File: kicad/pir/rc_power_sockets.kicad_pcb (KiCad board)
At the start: 2 copper layers, 50 x 50 mm, 32 parts, among them IC1 ATTINY85, J1 PIR, J2 433MHZ, J3 433MHZ, P1 ICSP, P2 ALT_PWR, Q1 NMOS, Q2 PMOS, SW1 SWITCH_INV, U1 MCP1755ST-3302E/DB

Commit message: Corrected the PMOS
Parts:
- R2: value 10K -> 100K
- moved Q2 6.33 mm to (130.4, 93.5), turned to 0 degrees
- moved R2 2.94 mm to (130.0, 98.1), turned to 180 degrees
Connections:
- Q2 pad 2: /SWITCH_POWER -> /POWER
- Q2 pad 3: /POWER -> /SWITCH_POWER
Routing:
- net /PBASE: track 30.3 -> 26.5 mm, vias 2 -> 0
- net /POWER: track 28.7 -> 25.2 mm
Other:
- board text added: "RC Power Sockets v1.1 - Sept 2016"
- board text removed: "RC Power Sockets v1.0 - March 2016"
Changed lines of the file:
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@@
     (links 58)
     (no_connects 0)
-    (area 116.525 58.475 171.308334 111.375)
+    (area 119.924999 59.924999 170.075001 110.075001)
     (thickness 1.6)
     (drawings 47)
-    (tracks 281)
+    (tracks 277)
     (zones 0)
     (modules 32)
@@
   )
   (module TO_SOT_Packages_SMD:SOT-23_Handsoldering (layer F.Cu)
-    (at 124.5 95.9 180)
+    (at 130.355 93.503)
     (descr "SOT-23, Handsoldering")
     (tags SOT-23)
     (attr smd)
-    (fp_text reference Q2 (at 0 4 180) (layer F.SilkS) hide
-      (effects (font (size 1 1) (thickness 0.15)))
-    )
-    (fp_text value PMOS (at 0.1 -3.6 180) (layer F.SilkS)
+    (fp_text reference Q2 (at 0 4) (layer F.SilkS) hide
+      (effects (font (size 1 1) (thickness 0.15)))
+    )
+    (fp_text value PMOS (at 0.1 -3.6) (layer F.SilkS)
       (effects (font (size 1 1) (thickness 0.15)))
     )
@@
     (fp_line (start 1.29916 -0.65024) (end 1.49982 -0.65024) (layer F.SilkS) (width 0.15))
     (fp_line (start 1.49982 -0.65024) (end 1.49982 0.0508) (layer F.SilkS) (width 0.15))
-    (pad 1 smd rect (at -0.95 1.50114 180) (size 0.8001 1.80086) (layers F.Cu F.Paste F.Mask)
+    (pad 1 smd rect (at -0.95 1.50114) (size 0.8001 1.80086) (layers F.Cu F.Paste F.Mask)
       (net 11 /PBASE))
-    (pad 2 smd rect (at 0.95 1.50114 180) (size 0.8001 1.80086) (layers F.Cu F.Paste F.Mask)
+    (pad 2 smd rect (at 0.95 1.50114) (size 0.8001 1.80086) (layers F.Cu F.Paste F.Mask)
+      (net 13 /POWER))
+    (pad 3 smd rect (at 0 -1.50114) (size 0.8001 1.80086) (layers F.Cu F.Paste F.Mask)
       (net 8 /SWITCH_POWER))
-    (pad 3 smd rect (at 0 -1.50114 180) (size 0.8001 1.80086) (layers F.Cu F.Paste F.Mask)
-      (net 13 /POWER))
     (model TO_SOT_Packages_SMD.3dshapes/SOT-23_Handsoldering.wrl
       (at (xyz 0 0 0))
@@
   )
   (module Resistors_SMD:R_0805_HandSoldering (layer F.Cu)
-    (at 128 95.9 90)
+    (at 129.974 98.075 180)
     (descr "Resistor SMD 0805, hand soldering")
     (tags "resistor 0805")
     (attr smd)
-    (fp_text reference R2 (at 0 2.2 180) (layer F.SilkS)
-      (effects (font (size 1 1) (thickness 0.15)))
-    )
-    (fp_text value 10K (at 3.4 0 180) (layer F.SilkS)
+    (fp_text reference R2 (at 3.556 0 360) (layer F.SilkS)
+      (effects (font (size 1 1) (thickness 0.15)))
+    )
+    (fp_text value 100K (at 0 -2.032 360) (layer F.SilkS)
       (effects (font (size 1 1) (thickness 0.15)))
     )
@@
     (fp_line (start 0.6 0.875) (end -0.6 0.875) (layer F.SilkS) (width 0.15))
     (fp_line (start -0.6 -0.875) (end 0.6 -0.875) (layer F.SilkS) (width 0.15))
-    (pad 1 smd rect (at -1.35 0 90) (size 1.5 1.3) (layers F.Cu F.Paste F.Mask)
+    (pad 1 smd rect (at -1.35 0 180) (size 1.5 1.3) (layers F.Cu F.Paste F.Mask)
       (net 13 /POWER))
-    (pad 2 smd rect (at 1.35 0 90) (size 1.5 1.3) (layers F.Cu F.Paste F.Mask)
+    (pad 2 smd rect (at 1.35 0 180) (size 1.5 1.3) (layers F.Cu F.Paste F.Mask)
       (net 11 /PBASE))
     (model Resistors_SMD.3dshapes/R_0805_HandSoldering.wrl
@@
     (effects (font (size 1 1) (thickness 0.15)) (justify mirror))
   )
-  (gr_text "RC Power Sockets v1.0  - March 2016" (at 144.6 61.3) (layer B.SilkS)
+  (gr_text "RC Power Sockets v1.1  - Sept 2016" (at 144.6 61.3) (layer B.SilkS)
     (effects (font (size 1 1) (thickness 0.15) italic) (justify mirror))
   )
@@
   (segment (start 165.28 97.44) (end 167.82 97.44) (width 0.406) (layer F.Cu) (net 7))
   (segment (start 162.4 94.56) (end 165.28 97.44) (width 0.406) (layer F.Cu) (net 7))
+  (segment (start 126 89.9) (end 128.10186 92.00186) (width 0.813) (layer F.Cu) (net 8))
+  (segment (start 128.10186 92.00186) (end 130.355 92.00186) (width 0.813) (layer F.Cu) (net 8))
   (segment (start 152.45 71.5) (end 152.45 73.44) (width 0.813) (layer F.Cu) (net 8))
   (segment (start 140.896 64.42) (end 137.34 64.42) (width 0.813) (layer F.Cu) (net 8))
@@
   (segment (start 155.5 70.588) (end 155.464 70.552) (width 0.813) (layer F.Cu) (net 8))
   (segment (start 126 84.698) (end 126 89.9) (width 0.813) (layer F.Cu) (net 8))
-  (segment (start 123.55 92.35) (end 123.55 94.39886) (width 0.813) (layer F.Cu) (net 8))
-  (segment (start 126 89.9) (end 123.55 92.35) (width 0.813) (layer F.Cu) (net 8))
   (segment (start 126 84.698) (end 126 84.838) (width 0.813) (layer F.Cu) (net 8))
   (segment (start 126 84.838) (end 126 81.4) (width 0.813) (layer F.Cu) (net 8))
@@
   (segment (start 144.44886 101.9) (end 144.15 102.19886) (width 0.406) (layer F.Cu) (net 10))
   (segment (start 147.05 105.1) (end 147.05 101.9) (width 0.406) (layer F.Cu) (net 10))
-  (segment (start 128 94.55) (end 130.55 94.55) (width 0.406) (layer F.Cu) (net 11))
-  (segment (start 143.2 106.9) (end 143.2 105.20114) (width 0.406) (layer F.Cu) (net 11))
-  (segment (start 142.4 107.7) (end 143.2 106.9) (width 0.406) (layer F.Cu) (net 11))
-  (segment (start 135.4 107.7) (end 142.4 107.7) (width 0.406) (layer F.Cu) (net 11))
-  (segment (start 133.4 105.7) (end 135.4 107.7) (width 0.406) (layer F.Cu) (net 11))
-  (via (at 133.4 105.7) (size 0.75) (drill 0.4) (layers F.Cu B.Cu) (net 11))
-  (segment (start 130.6 102.9) (end 133.4 105.7) (width 0.406) (layer B.Cu) (net 11))
-  (segment (start 130.6 101.3) (end 130.6 102.9) (width 0.406) (layer B.Cu) (net 11))
-  (segment (start 130.6 94.5) (end 130.6 101.3) (width 0.406) (layer B.Cu) (net 11))
-  (via (at 130.6 94.5) (size 0.75) (drill 0.4) (layers F.Cu B.Cu) (net 11))
-  (segment (start 130.55 94.55) (end 130.6 94.5) (width 0.406) (layer F.Cu) (net 11))
-  (segment (start 125.45 94.39886) (end 127.84886 94.39886) (width 0.406) (layer F.Cu) (net 11))
-  (segment (start 127.84886 94.39886) (end 128 94.55) (width 0.406) (layer F.Cu) (net 11))
+  (segment (start 143.2 105.20114) (end 143.2 106.9) (width 0.406) (layer F.Cu) (net 11))
+  (segment (start 143.2 106.9) (end 142.4 107.7) (width 0.406) (layer F.Cu) (net 11))
+  (segment (start 142.4 107.7) (end 134.031 107.7) (width 0.406) (layer F.Cu) (net 11))
+  (segment (start 134.031 107.7) (end 128.624 102.293) (width 0.406) (layer F.Cu) (net 11))
+  (segment (start 128.624 102.293) (end 128.624 98.075) (width 0.406) (layer F.Cu) (net 11))
+  (segment (start 129.413 96.23) (end 129.413 95.01214) (width 0.406) (layer F.Cu) (net 11))
+  (segment (start 129.413 95.01214) (end 129.405 95.00414) (width 0.406) (layer F.Cu) (net 11))
+  (segment (start 128.624 98.075) (end 128.624 97.019) (width 0.406) (layer F.Cu) (net 11))
+  (segment (start 128.624 97.019) (end 129.413 96.23) (width 0.406) (layer F.Cu) (net 11))
   (segment (start 157 105.4336) (end 158.016 105.4336) (width 0.406) (layer F.Cu) (net 12))
   (segment (start 158.016 105.4336) (end 161.724 101.7256) (width 0.406) (layer F.Cu) (net 12))
@@
   (segment (start 155.141 105.441) (end 151.6 101.9) (width 0.406) (layer F.Cu) (net 12))
   (segment (start 151.6 101.9) (end 149.75 101.9) (width 0.406) (layer F.Cu) (net 12))
+  (segment (start 131.324 98.075) (end 131.324 95.02314) (width 0.813) (layer F.Cu) (net 13))
+  (segment (start 131.324 95.02314) (end 131.305 95.00414) (width 0.813) (layer F.Cu) (net 13))
+  (segment (start 136.959 95.027) (end 133.911 98.075) (width 0.813) (layer F.Cu) (net 13))
+  (segment (start 133.911 98.075) (end 131.324 98.075) (width 0.813) (layer F.Cu) (net 13))
+  (segment (start 136.959 92.36) (end 136.959 95.027) (width 0.813) (layer F.Cu) (net 13))
   (segment (start 147.5 94.9) (end 147.5 93.249) (width 0.813) (layer F.Cu) (net 13))
   (segment (start 147.5 93.249) (end 146.611 92.36) (width 0.813) (layer F.Cu) (net 13))
   (segment (start 146.611 92.36) (end 136.959 92.36) (width 0.813) (layer F.Cu) (net 13))
-  (segment (start 136.959 92.36) (end 136.959 95.027) (width 0.813) (layer F.Cu) (net 13))
-  (segment (start 136.959 95.027) (end 134.736 97.25) (width 0.813) (layer F.Cu) (net 13))
-  (segment (start 134.736 97.25) (end 128 97.25) (width 0.813) (layer F.Cu) (net 13))
-  (segment (start 124.5 97.40114) (end 127.84886 97.40114) (width 0.813) (layer F.Cu) (net 13))
-  (segment (start 127.84886 97.40114) (end 128 97.25) (width 0.813) (layer F.Cu) (net 13))
   (segment (start 168 73.94902) (end 165.80098 73.94902) (width 0.406) (layer B.Cu) (net 14))
   (segment (start 165.80098 73.94902) (end 165.5 74.25) (width 0.406) (layer B.Cu) (net 14))

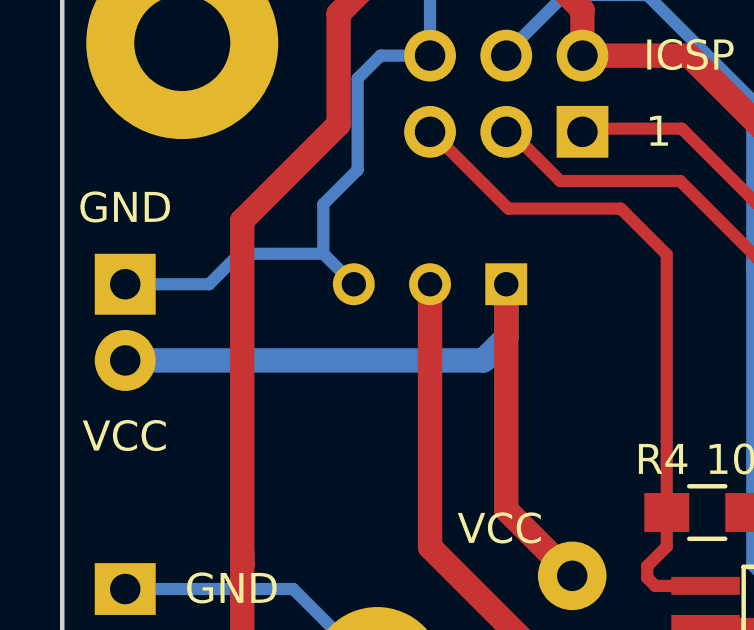
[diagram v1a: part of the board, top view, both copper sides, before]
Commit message: Capacitor on the power input
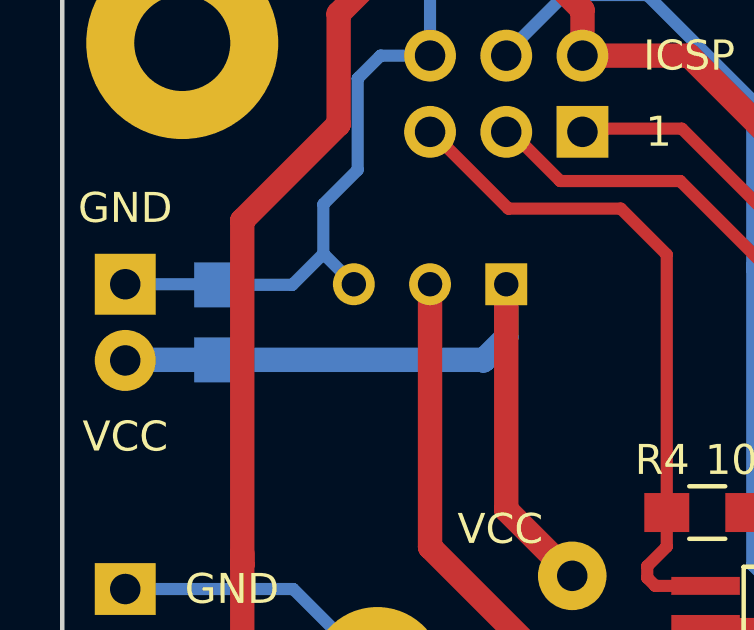
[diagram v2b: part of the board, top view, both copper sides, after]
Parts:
- added C4: 10uF, Capacitors_SMD:C_0805_HandSoldering, B.Cu at (125.0, 73.3)
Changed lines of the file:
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@@
 (kicad_pcb (version 4) (host pcbnew 4.0.1-stable)
   (general
-    (links 58)
+    (links 60)
     (no_connects 0)
     (area 119.924999 59.924999 170.075001 110.075001)
     (thickness 1.6)
     (drawings 47)
-    (tracks 277)
+    (tracks 282)
     (zones 0)
-    (modules 32)
+    (modules 33)
     (nets 18)
   )
@@
       (net 17 /VCC_SWITCHED))
   )
+  (module Capacitors_SMD:C_0805_HandSoldering (layer B.Cu)
+    (at 125.021 73.31 90)
+    (descr "Capacitor SMD 0805, hand soldering")
+    (tags "capacitor 0805")
+    (attr smd)
+    (fp_text reference C4 (at 3.048 0 180) (layer B.SilkS)
+      (effects (font (size 1 1) (thickness 0.15)) (justify mirror))
+    )
+    (fp_text value 10uF (at 0 1.778 90) (layer B.SilkS)
+      (effects (font (size 1 1) (thickness 0.15)) (justify mirror))
+    )
+    (fp_line (start -2.3 1) (end 2.3 1) (layer B.CrtYd) (width 0.05))
+    (fp_line (start -2.3 -1) (end 2.3 -1) (layer B.CrtYd) (width 0.05))
+    (fp_line (start -2.3 1) (end -2.3 -1) (layer B.CrtYd) (width 0.05))
+    (fp_line (start 2.3 1) (end 2.3 -1) (layer B.CrtYd) (width 0.05))
+    (fp_line (start 0.5 0.85) (end -0.5 0.85) (layer B.SilkS) (width 0.15))
+    (fp_line (start -0.5 -0.85) (end 0.5 -0.85) (layer B.SilkS) (width 0.15))
+    (pad 1 smd rect (at -1.25 0 90) (size 1.5 1.25) (layers B.Cu B.Paste B.Mask)
+      (net 16 VCC))
+    (pad 2 smd rect (at 1.25 0 90) (size 1.5 1.25) (layers B.Cu B.Paste B.Mask)
+      (net 1 GND))
+    (model Capacitors_SMD.3dshapes/C_0805_HandSoldering.wrl
+      (at (xyz 0 0 0))
+      (scale (xyz 1 1 1))
+      (rotate (xyz 0 0 0))
+    )
+  )
   (gr_text POT (at 167.693 92.36) (layer F.SilkS)
     (effects (font (size 1 1) (thickness 0.15)))
@@
     (effects (font (size 1 1) (thickness 0.15)) (justify mirror))
   )
-  (gr_text "RC Power Sockets v1.1  - Sept 2016" (at 144.6 61.3) (layer B.SilkS)
+  (gr_text "RC Power Sockets v1.1 - Sept 2016" (at 144.6 61.3) (layer B.SilkS)
     (effects (font (size 1 1) (thickness 0.15) italic) (justify mirror))
   )
@@
   (gr_line (start 170 60) (end 170 110) (angle 90) (layer Edge.Cuts) (width 0.15))
   (gr_line (start 120 60) (end 170 60) (angle 90) (layer Edge.Cuts) (width 0.15))
+  (segment (start 125.021 72.06) (end 127.668 72.06) (width 0.406) (layer B.Cu) (net 1))
+  (segment (start 127.668 72.06) (end 128.704 71.024) (width 0.406) (layer B.Cu) (net 1))
+  (segment (start 122.1 72.04) (end 125.001 72.04) (width 0.406) (layer B.Cu) (net 1))
+  (segment (start 125.001 72.04) (end 125.021 72.06) (width 0.406) (layer B.Cu) (net 1))
+  (segment (start 124.894 72.04) (end 124.914 72.06) (width 0.406) (layer B.Cu) (net 1))
   (segment (start 141.825 85.905) (end 139.477 85.905) (width 0.406) (layer F.Cu) (net 1))
   (segment (start 139.477 85.905) (end 138.991 86.391) (width 0.406) (layer F.Cu) (net 1))
@@
   (segment (start 135.701 90.201) (end 134.177 88.677) (width 0.406) (layer F.Cu) (net 1))
   (segment (start 129.72 72.04) (end 128.704 71.024) (width 0.406) (layer B.Cu) (net 1))
-  (segment (start 128.704 71.024) (end 125.91 71.024) (width 0.406) (layer B.Cu) (net 1))
-  (segment (start 124.894 72.04) (end 122.1 72.04) (width 0.406) (layer B.Cu) (net 1))
-  (segment (start 125.91 71.024) (end 124.894 72.04) (width 0.406) (layer B.Cu) (net 1))
   (segment (start 130.609 64.42) (end 132.26 64.42) (width 0.406) (layer B.Cu) (net 1))
   (segment (start 129.847 65.182) (end 130.609 64.42) (width 0.406) (layer B.Cu) (net 1))
@@
   (segment (start 146.8 102) (end 137 102) (width 0.813) (layer B.Cu) (net 15))
   (segment (start 152 96.8) (end 146.8 102) (width 0.813) (layer B.Cu) (net 15))
+  (segment (start 134.038 74.58) (end 134.018 74.56) (width 0.813) (layer B.Cu) (net 16))
+  (segment (start 134.018 74.56) (end 125.021 74.56) (width 0.813) (layer B.Cu) (net 16))
+  (segment (start 125.021 74.56) (end 122.12 74.56) (width 0.813) (layer B.Cu) (net 16))
+  (segment (start 122.12 74.56) (end 122.1 74.58) (width 0.813) (layer B.Cu) (net 16))
   (segment (start 134.8 72.04) (end 134.8 79.56) (width 0.813) (layer F.Cu) (net 16))
   (segment (start 134.8 79.56) (end 137 81.76) (width 0.813) (layer F.Cu) (net 16))
-  (segment (start 122.1 74.58) (end 134.038 74.58) (width 0.813) (layer B.Cu) (net 16))
   (segment (start 134.8 73.818) (end 134.8 72.04) (width 0.813) (layer B.Cu) (net 16))
   (segment (start 134.038 74.58) (end 134.8 73.818) (width 0.813) (layer B.Cu) (net 16))

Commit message: Tiny logo
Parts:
- added REF**: TheApiLogoTiny, theapi_footprints:TheApiLogoTiny, F.Cu at (129.3, 105.1)
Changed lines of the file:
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@@
     (tracks 282)
     (zones 0)
-    (modules 33)
+    (modules 34)
     (nets 18)
   )
@@
     )
   )
+  (module theapi_footprints:TheApiLogoTiny (layer F.Cu)
+    (at 129.339 105.06)
+    (fp_text reference REF** (at 0 0.5) (layer F.SilkS) hide
+      (effects (font (size 1 1) (thickness 0.15)))
+    )
+    (fp_text value TheApiLogoTiny (at 0 -0.5) (layer F.Fab) hide
+      (effects (font (size 1 1) (thickness 0.15)))
+    )
+    (fp_line (start 0.26 4.07) (end 0.42 3.55) (layer F.Mask) (width 0.1016))
+    (fp_line (start 0.3 3.85) (end 0.26 4.07) (layer F.Mask) (width 0.1016))
+    (fp_line (start 0.18 3.57) (end 0.3 3.85) (layer F.Mask) (width 0.1016))
+    (fp_line (start -0.04 3.27) (end 0.18 3.57) (layer F.Mask) (width 0.1016))
+    (fp_line (start -0.13 2.84) (end -0.04 3.27) (layer F.Mask) (width 0.1016))
+    (fp_line (start 0.24 2.85) (end 0.24 2.68) (layer F.Mask) (width 0.1016))
+    (fp_line (start 0.26 2.95) (end 0.24 2.85) (layer F.Mask) (width 0.1016))
+    (fp_line (start 0.21 3.04) (end 0.26 2.95) (layer F.Mask) (width 0.1016))
+    (fp_line (start 0.09 3.07) (end 0.21 3.04) (layer F.Mask) (width 0.1016))
+    (fp_line (start -0.03 2.94) (end 0.09 3.07) (layer F.Mask) (width 0.1016))
+    (fp_line (start -0.1 2.75) (end -0.03 2.94) (layer F.Mask) (width 0.1016))
+    (fp_line (start 0.42 2.75) (end 0.33 2.62) (layer F.Mask) (width 0.1016))
+    (fp_line (start 0.55 2.78) (end 0.42 2.75) (layer F.Mask) (width 0.1016))
+    (fp_line (start 0.66 2.74) (end 0.55 2.78) (layer F.Mask) (width 0.1016))
+    (fp_line (start 0.7 2.64) (end 0.66 2.74) (layer F.Mask) (width 0.1016))
+    (fp_line (start 0.7 2.5) (end 0.7 2.64) (layer F.Mask) (width 0.1016))
+    (fp_line (start 0.6 2.36) (end 0.7 2.5) (layer F.Mask) (width 0.1016))
+    (fp_line (start 0.42 2.25) (end 0.6 2.36) (layer F.Mask) (width 0.1016))
+    (fp_line (start 0.52 2.22) (end 0.42 2.22) (layer F.Mask) (width 0.1016))
+    (fp_line (start 0.67 2.21) (end 0.52 2.22) (layer F.Mask) (width 0.1016))
+    (fp_line (start 0.77 2.14) (end 0.67 2.21) (layer F.Mask) (width 0.1016))
+    (fp_line (start 0.75 1.99) (end 0.77 2.14) (layer F.Mask) (width 0.1016))
+    (fp_line (start 0.64 1.89) (end 0.75 1.99) (layer F.Mask) (width 0.1016))
+    (fp_line (start 0.27 1.9) (end 0.64 1.89) (layer F.Mask) (width 0.1016))
+    (fp_line (start 0.39 1.77) (end 0.3 1.91) (layer F.Mask) (width 0.1016))
+    (fp_line (start 0.41 1.66) (end 0.39 1.77) (layer F.Mask) (width 0.1016))
+    (fp_line (start 0.36 1.55) (end 0.41 1.66) (layer F.Mask) (width 0.1016))
+    (fp_line (start 0.19 1.52) (end 0.36 1.55) (layer F.Mask) (width 0.1016))
+    (fp_line (start 0.03 1.58) (end 0.19 1.52) (layer F.Mask) (width 0.1016))
+    (fp_line (start -0.06 1.85) (end 0.03 1.58) (layer F.Mask) (width 0.1016))
+    (fp_line (start -0.16 2.76) (end -0.17 2.73) (layer F.Mask) (width 0.1016))
+    (fp_line (start -0.13 2.74) (end -0.16 2.76) (layer F.Mask) (width 0.1016))
+    (fp_line (start -0.15 2.76) (end -0.13 2.74) (layer F.Mask) (width 0.1016))
+    (fp_line (start -0.17 2.87) (end -0.15 2.76) (layer F.Mask) (width 0.1016))
+    (fp_line (start -0.23 2.98) (end -0.17 2.87) (layer F.Mask) (width 0.1016))
+    (fp_line (start -0.35 3.02) (end -0.23 2.98) (layer F.Mask) (width 0.1016))
+    (fp_line (start -0.46 2.98) (end -0.35 3.02) (layer F.Mask) (width 0.1016))
+    (fp_line (start -0.47 2.79) (end -0.46 2.98) (layer F.Mask) (width 0.1016))
+    (fp_line (start -0.39 2.59) (end -0.47 2.79) (layer F.Mask) (width 0.1016))
+    (fp_line (start -0.66 2.63) (end -0.41 2.57) (layer F.Mask) (width 0.1016))
+    (fp_line (start -0.78 2.55) (end -0.66 2.63) (layer F.Mask) (width 0.1016))
+    (fp_line (start -0.82 2.42) (end -0.78 2.55) (layer F.Mask) (width 0.1016))
+    (fp_line (start -0.73 2.27) (end -0.82 2.42) (layer F.Mask) (width 0.1016))
+    (fp_line (start -0.46 2.22) (end -0.73 2.27) (layer F.Mask) (width 0.1016))
+    (fp_line (start -0.68 2.1) (end -0.47 2.15) (layer F.Mask) (width 0.1016))
+    (fp_line (start -0.79 1.93) (end -0.68 2.1) (layer F.Mask) (width 0.1016))
+    (fp_line (start -0.68 1.74) (end -0.79 1.93) (layer F.Mask) (width 0.1016))
+    (fp_line (start -0.4 1.67) (end -0.68 1.74) (layer F.Mask) (width 0.1016))
+    (fp_line (start -0.13 1.81) (end -0.4 1.67) (layer F.Mask) (width 0.1016))
+    (fp_line (start 0.04 2.48) (end 0.16 2.39) (layer F.Mask) (width 0.0762))
+    (fp_line (start -0.09 2.49) (end 0.04 2.48) (layer F.Mask) (width 0.0762))
+    (fp_line (start -0.21 2.42) (end -0.09 2.49) (layer F.Mask) (width 0.0762))
+    (fp_circle (center -0.16 2.2) (end -0.13 2.21) (layer F.Mask) (width 0.15))
+    (fp_circle (center -0.02 2.28) (end 0.39 2.28) (layer F.Mask) (width 0.127))
+    (fp_circle (center 0.12 2.2) (end 0.15 2.21) (layer F.Mask) (width 0.15))
+  )
   (gr_text POT (at 167.693 92.36) (layer F.SilkS)
